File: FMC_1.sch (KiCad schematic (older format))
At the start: 14 parts, among them P1 SAMTEC_ASP-134603-01

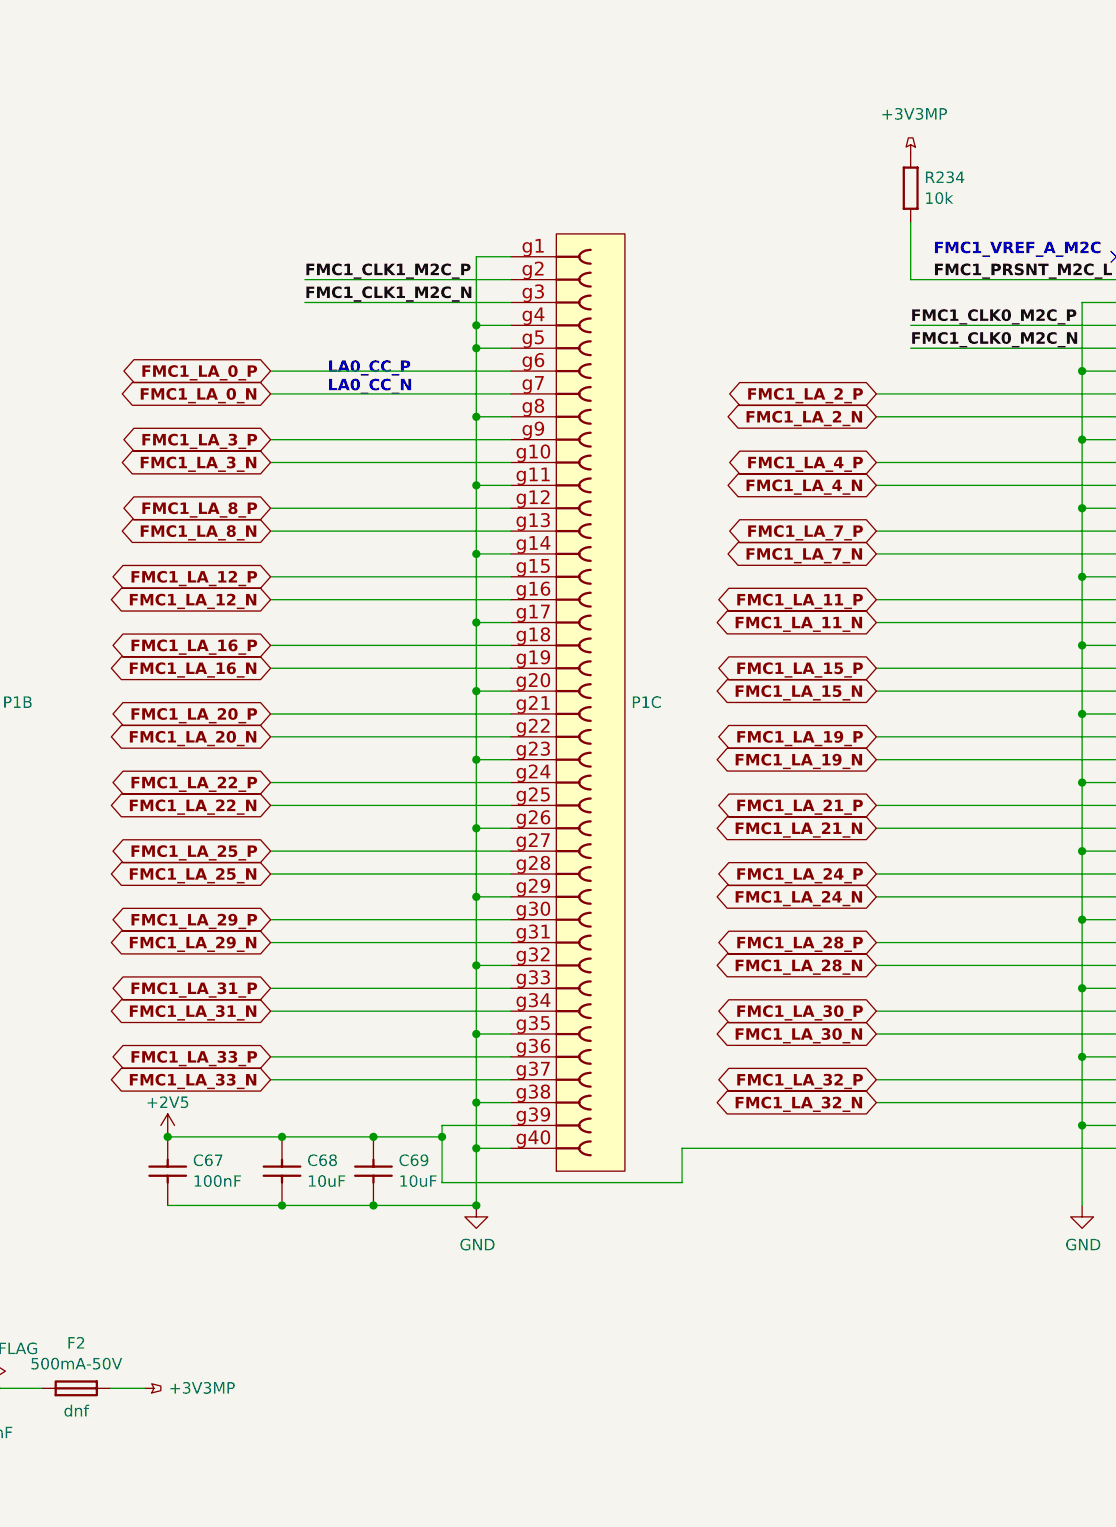
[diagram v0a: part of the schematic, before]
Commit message: SCH: rename +3.3VP, 3V3PM and +3V3MP to +3V3P
  * all of them refer to the same net
  * to make confusion perfect, all 3 power symbols on the schematic
    were an instance of the symbol `+3.3VP` with different
    value attributes
  * renamed the `+3.3VP` symbol to `+3V3P` for naming consistency
  * SCH: replaced all power symbols on the net by the new one
  * PCB: still needs to be synced up, as the net name has changed
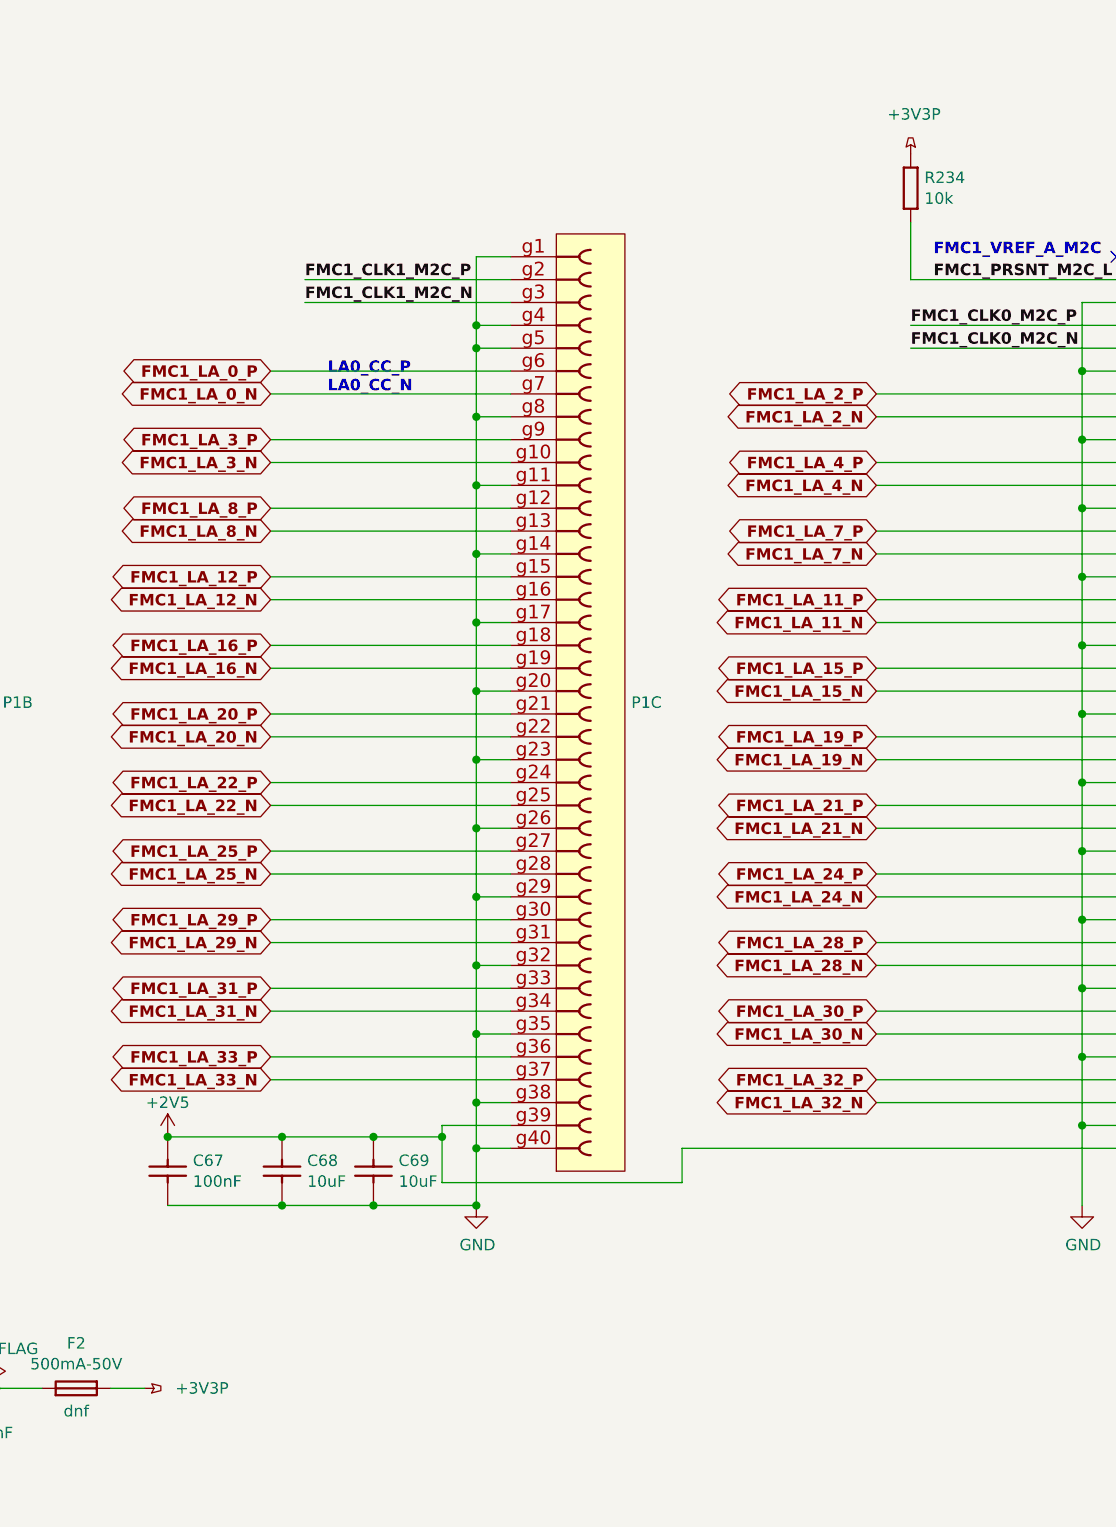
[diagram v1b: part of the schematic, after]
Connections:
- net +3.3VP renamed +3V3P
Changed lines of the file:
@@
 $EndComp
 $Comp
-L power:+3.3VP #PWR?
+L power:+3V3P #PWR?
 U 1 1 5DD348B7
 P 7000 6600
@@
 AR Path="/5DD348B7" Ref="#PWR0550"  Part="1"
 F 0 "#PWR0550" H 7000 6450 50  0001 C CNN
-F 1 "+3V3MP" V 7000 6850 50  0000 C CNN
+F 1 "+3V3P" V 7000 6850 50  0000 C CNN
 F 2 "" H 7000 6600 50  0001 C CNN
 F 3 "" H 7000 6600 50  0001 C CNN
@@
 	10350 1750 11250 1750
 $Comp
-L power:+3.3VP #PWR?
+L power:+3V3P #PWR?
 U 1 1 5E9F763B
 P 10350 1200
@@
 AR Path="/5E9F763B" Ref="#PWR0503"  Part="1"
 F 0 "#PWR0503" H 10350 1050 50  0001 C CNN
-F 1 "+3V3MP" H 10365 1373 50  0000 C CNN
+F 1 "+3V3P" H 10365 1373 50  0000 C CNN
 F 2 "" H 10350 1200 50  0001 C CNN
 F 3 "" H 10350 1200 50  0001 C CNN

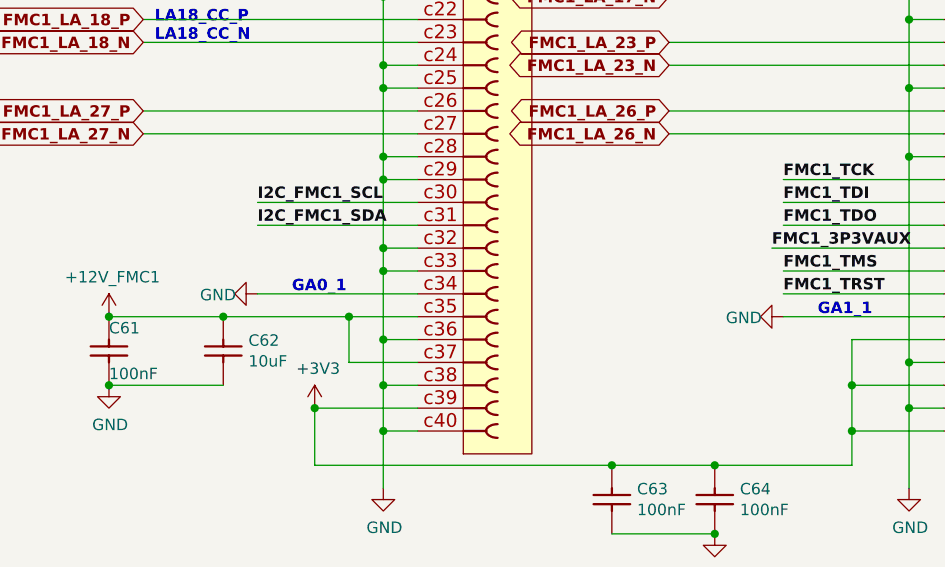
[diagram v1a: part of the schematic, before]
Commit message: Add 300 Ohm series resistors to GA pins
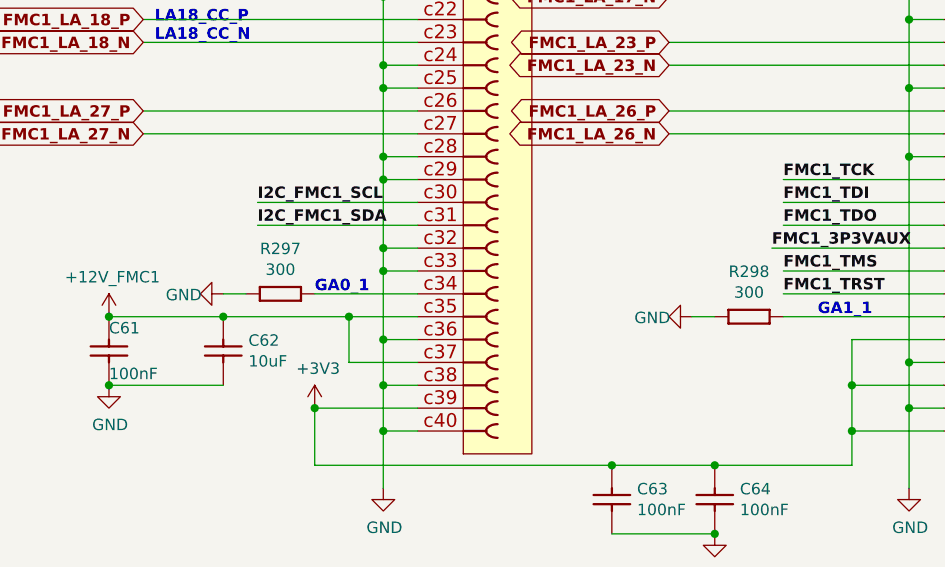
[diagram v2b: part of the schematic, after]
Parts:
- added R297, R298: R0402_300R_1%_0.0625W_100PPM, Resistors SMD:RESC1005X40N, symbol Resistors_SMD:R0402_300R_1%_0.0625W_100PPM
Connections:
- net GND: now also R297.1, R298.1; no longer P1.c34, P1.d35
- new net: P1.c34, R297.2
- new net: P1.d35, R298.2
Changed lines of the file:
@@
 Connection ~ 5450 5550
-Wire Wire Line
-	2850 4950 3550 4950
 Wire Wire Line
 	2850 4550 3550 4550
@@
 Wire Wire Line
 	5150 4850 5850 4850
-Wire Wire Line
-	5150 5050 5850 5050
 Text Notes 4650 3650 0    50   ~ 10
 LA17_CC_P\nLA17_CC_N
@@
 L power:GND #PWR?
 U 1 1 5D17E89A
-P 2850 4950
+P 2700 4950
 AR Path="/5BD32060/5D17E89A" Ref="#PWR?"  Part="1"
 AR Path="/5BD31F9A/5D17E89A" Ref="#PWR0125"  Part="1"
 AR Path="/5BD31F9F/5D17E89A" Ref="#PWR?"  Part="1"
 AR Path="/5D17E89A" Ref="#PWR?"  Part="1"
-F 0 "#PWR0125" H 2850 4700 50  0001 C CNN
-F 1 "GND" V 2855 4777 50  0000 C CNN
-F 2 "" H 2850 4950 50  0001 C CNN
-F 3 "" H 2850 4950 50  0001 C CNN
-	1    2850 4950
+F 0 "#PWR0125" H 2700 4700 50  0001 C CNN
+F 1 "GND" V 2705 4777 50  0000 C CNN
+F 2 "" H 2700 4950 50  0001 C CNN
+F 3 "" H 2700 4950 50  0001 C CNN
+	1    2700 4950
 	0    1    1    0
 $EndComp
@@
 L power:GND #PWR?
 U 1 1 5D19449D
-P 5150 5050
+P 4750 5050
 AR Path="/5BD32060/5D19449D" Ref="#PWR?"  Part="1"
 AR Path="/5BD31F9A/5D19449D" Ref="#PWR0215"  Part="1"
 AR Path="/5BD31F9F/5D19449D" Ref="#PWR?"  Part="1"
 AR Path="/5D19449D" Ref="#PWR?"  Part="1"
-F 0 "#PWR0215" H 5150 4800 50  0001 C CNN
-F 1 "GND" V 5155 4877 50  0000 C CNN
-F 2 "" H 5150 5050 50  0001 C CNN
-F 3 "" H 5150 5050 50  0001 C CNN
-	1    5150 5050
+F 0 "#PWR0215" H 4750 4800 50  0001 C CNN
+F 1 "GND" V 4755 4877 50  0000 C CNN
+F 2 "" H 4750 5050 50  0001 C CNN
+F 3 "" H 4750 5050 50  0001 C CNN
+	1    4750 5050
 	0    1    1    0
 $EndComp
-Text Notes 3000 4950 0    50   ~ 10
+Text Notes 3100 4950 0    50   ~ 10
 GA0_1
 Text Notes 5300 5050 0    50   ~ 10
@@
 Wire Wire Line
 	6350 6600 6550 6600
+$Comp
+L Resistors_SMD:R0402_300R_1%_0.0625W_100PPM R297
+U 1 1 5EBC4ACC
+P 2800 4950
+F 0 "R297" H 2950 5147 50  0000 C CNN
+F 1 "R0402_300R_1%_0.0625W_100PPM" H 2800 4755 50  0001 L CNN
+F 2 "Resistors SMD:RESC1005X40N" H 2800 4680 50  0001 L CNN
+F 3 " " H 2800 4605 50  0001 L CNN
+F 4 "300" H 2950 5056 50  0000 C CNN "Val"
+F 5 "R0402_300R_1%_0.0625W_100PPM" H 2800 4530 50  0001 L CNN "Part Number"
+F 6 "Resistor - 1%" H 2800 4455 50  0001 L CNN "Library Ref"
+F 7 "SchLib\\Resistors.SchLib" H 2800 4380 50  0001 L CNN "Library Path"
+F 8 "300" H 2800 4305 50  0001 L CNN "Comment"
+F 9 "Standard" H 2800 4230 50  0001 L CNN "Component Kind"
+F 10 "Standard" H 2800 4155 50  0001 L CNN "Component Type"
+F 11 " " H 2800 4080 50  0001 L CNN "PackageDescription"
+F 12 "2" H 2800 4005 50  0001 L CNN "Pin Count"
+F 13 "PcbLib\\Resistors SMD.PcbLib" H 2800 3930 50  0001 L CNN "Footprint Path"
+F 14 "RESC1005X40N" H 2800 3855 50  0001 L CNN "Footprint Ref"
+F 15 "Not Recommended" H 2800 3780 50  0001 L CNN "Status"
+F 16 "0.0625W" H 2800 3705 50  0001 L CNN "Power"
+F 17 "±100ppm/°C" H 2800 3630 50  0001 L CNN "TC"
+F 18 " " H 2800 3555 50  0001 L CNN "Voltage"
+F 19 "±1%" H 2800 3480 50  0001 L CNN "Tolerance"
+F 20 "General Purpose Thick Film Chip Resistor" H 2800 3405 50  0001 L CNN "Part Description"
+F 21 "GENERIC" H 2800 3330 50  0001 L CNN "Manufacturer"
+F 22 "R0402_300R_1%_0.0625W_100PPM" H 2800 3255 50  0001 L CNN "Manufacturer Part Number"
+F 23 "0402" H 2800 3180 50  0001 L CNN "Case"
+F 24 "No" H 2800 3105 50  0001 L CNN "PressFit"
+F 25 "Yes" H 2800 3030 50  0001 L CNN "Mounted"
+F 26 " " H 2800 2955 50  0001 L CNN "Sense Comment"
+F 27 "No" H 2800 2880 50  0001 L CNN "Sense"
+F 28 " " H 2800 2805 50  0001 L CNN "Status Comment"
+F 29 "No" H 2800 2730 50  0001 L CNN "Socket"
+F 30 "Yes" H 2800 2655 50  0001 L CNN "SMD"
+F 31 " " H 2800 2580 50  0001 L CNN "ComponentHeight"
+F 32 "YAGEO PHYCOMP" H 2800 2505 50  0001 L CNN "Manufacturer1 Example"
+F 33 "232270673001L" H 2800 2430 50  0001 L CNN "Manufacturer1 Part Number"
+F 34 "0.4mm" H 2800 2355 50  0001 L CNN "Manufacturer1 ComponentHeight"
+F 35 "CERN DEM JLC" H 2800 2280 50  0001 L CNN "Author"
+F 36 "12/03/07 00:00:00" H 2800 2205 50  0001 L CNN "CreateDate"
+F 37 "10/17/12 00:00:00" H 2800 2130 50  0001 L CNN "LatestRevisionDate"
+F 38 "Resistors SMD" H 2800 2055 50  0001 L CNN "Database Table Name"
+F 39 "Resistors.DbLib" H 2800 1980 50  0001 L CNN "Library Name"
+F 40 "Resistors SMD" H 2800 1905 50  0001 L CNN "Footprint Library"
+F 41 "This work is licensed under the Creative Commons CC-BY-SA 4.0 License. To the extent that circuit schematics that use Licensed Material can be considered to be ‘Adapted Material’, then the copyright holder waives article 3.b of the license with respect to these schematics." H 2800 1830 50  0001 L CNN "License"
+	1    2800 4950
+	1    0    0    -1
+$EndComp
+Wire Wire Line
+	2700 4950 2800 4950
+Wire Wire Line
+	3100 4950 3550 4950
+$Comp
+L Resistors_SMD:R0402_300R_1%_0.0625W_100PPM R298
+U 1 1 5ECB9FE8
+P 4850 5050
+F 0 "R298" H 5000 5247 50  0000 C CNN
+F 1 "R0402_300R_1%_0.0625W_100PPM" H 4850 4855 50  0001 L CNN
+F 2 "Resistors SMD:RESC1005X40N" H 4850 4780 50  0001 L CNN
+F 3 " " H 4850 4705 50  0001 L CNN
+F 4 "300" H 5000 5156 50  0000 C CNN "Val"
+F 5 "R0402_300R_1%_0.0625W_100PPM" H 4850 4630 50  0001 L CNN "Part Number"
+F 6 "Resistor - 1%" H 4850 4555 50  0001 L CNN "Library Ref"
+F 7 "SchLib\\Resistors.SchLib" H 4850 4480 50  0001 L CNN "Library Path"
+F 8 "300" H 4850 4405 50  0001 L CNN "Comment"
+F 9 "Standard" H 4850 4330 50  0001 L CNN "Component Kind"
+F 10 "Standard" H 4850 4255 50  0001 L CNN "Component Type"
+F 11 " " H 4850 4180 50  0001 L CNN "PackageDescription"
+F 12 "2" H 4850 4105 50  0001 L CNN "Pin Count"
+F 13 "PcbLib\\Resistors SMD.PcbLib" H 4850 4030 50  0001 L CNN "Footprint Path"
+F 14 "RESC1005X40N" H 4850 3955 50  0001 L CNN "Footprint Ref"
+F 15 "Not Recommended" H 4850 3880 50  0001 L CNN "Status"
+F 16 "0.0625W" H 4850 3805 50  0001 L CNN "Power"
+F 17 "±100ppm/°C" H 4850 3730 50  0001 L CNN "TC"
+F 18 " " H 4850 3655 50  0001 L CNN "Voltage"
+F 19 "±1%" H 4850 3580 50  0001 L CNN "Tolerance"
+F 20 "General Purpose Thick Film Chip Resistor" H 4850 3505 50  0001 L CNN "Part Description"
+F 21 "GENERIC" H 4850 3430 50  0001 L CNN "Manufacturer"
+F 22 "R0402_300R_1%_0.0625W_100PPM" H 4850 3355 50  0001 L CNN "Manufacturer Part Number"
+F 23 "0402" H 4850 3280 50  0001 L CNN "Case"
+F 24 "No" H 4850 3205 50  0001 L CNN "PressFit"
+F 25 "Yes" H 4850 3130 50  0001 L CNN "Mounted"
+F 26 " " H 4850 3055 50  0001 L CNN "Sense Comment"
+F 27 "No" H 4850 2980 50  0001 L CNN "Sense"
+F 28 " " H 4850 2905 50  0001 L CNN "Status Comment"
+F 29 "No" H 4850 2830 50  0001 L CNN "Socket"
+F 30 "Yes" H 4850 2755 50  0001 L CNN "SMD"
+F 31 " " H 4850 2680 50  0001 L CNN "ComponentHeight"
+F 32 "YAGEO PHYCOMP" H 4850 2605 50  0001 L CNN "Manufacturer1 Example"
+F 33 "232270673001L" H 4850 2530 50  0001 L CNN "Manufacturer1 Part Number"
+F 34 "0.4mm" H 4850 2455 50  0001 L CNN "Manufacturer1 ComponentHeight"
+F 35 "CERN DEM JLC" H 4850 2380 50  0001 L CNN "Author"
+F 36 "12/03/07 00:00:00" H 4850 2305 50  0001 L CNN "CreateDate"
+F 37 "10/17/12 00:00:00" H 4850 2230 50  0001 L CNN "LatestRevisionDate"
+F 38 "Resistors SMD" H 4850 2155 50  0001 L CNN "Database Table Name"
+F 39 "Resistors.DbLib" H 4850 2080 50  0001 L CNN "Library Name"
+F 40 "Resistors SMD" H 4850 2005 50  0001 L CNN "Footprint Library"
+F 41 "This work is licensed under the Creative Commons CC-BY-SA 4.0 License. To the extent that circuit schematics that use Licensed Material can be considered to be ‘Adapted Material’, then the copyright holder waives article 3.b of the license with respect to these schematics." H 4850 1930 50  0001 L CNN "License"
+	1    4850 5050
+	1    0    0    -1
+$EndComp
+Wire Wire Line
+	4750 5050 4850 5050
+Wire Wire Line
+	5150 5050 5850 5050
 $EndSCHEMATC

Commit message: change R297 - R300 to 240 Ohm
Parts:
- R297, R298: value R0402_300R_1%_0.0625W_100PPM -> R0402_240R_1%_0.0625W_100PPM; footprint Resistors SMD:RESC1005X40N -> Marble:RESC1005X40N; symbol Resistors_SMD:R0402_300R_1%_0.0625W_100PPM -> Resistors_SMD:R0402_240R_1%_0.0625W_100PPM; Comment 300 -> 240; Manufacturer Part Number R0402_300R_1%_0.0625W_100PPM -> R0402_240R_1%_0.0625W_100PPM; Manufacturer1 Part Number 232270673001L -> 232270672401L; Part Number R0402_300R_1%_0.0625W_100PPM -> R0402_240R_1%_0.0625W_100PPM; Val 300 -> 240
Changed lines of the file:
@@
 	6350 6600 6550 6600
 $Comp
-L Resistors_SMD:R0402_300R_1%_0.0625W_100PPM R297
+L Resistors_SMD:R0402_240R_1%_0.0625W_100PPM R297
 U 1 1 5EBC4ACC
 P 2800 4950
 F 0 "R297" H 2950 5147 50  0000 C CNN
-F 1 "R0402_300R_1%_0.0625W_100PPM" H 2800 4755 50  0001 L CNN
-F 2 "Resistors SMD:RESC1005X40N" H 2800 4680 50  0001 L CNN
+F 1 "R0402_240R_1%_0.0625W_100PPM" H 2800 4755 50  0001 L CNN
+F 2 "Marble:RESC1005X40N" H 2800 4680 50  0001 L CNN
 F 3 " " H 2800 4605 50  0001 L CNN
-F 4 "300" H 2950 5056 50  0000 C CNN "Val"
-F 5 "R0402_300R_1%_0.0625W_100PPM" H 2800 4530 50  0001 L CNN "Part Number"
+F 4 "240" H 2950 5056 50  0000 C CNN "Val"
+F 5 "R0402_240R_1%_0.0625W_100PPM" H 2800 4530 50  0001 L CNN "Part Number"
 F 6 "Resistor - 1%" H 2800 4455 50  0001 L CNN "Library Ref"
 F 7 "SchLib\\Resistors.SchLib" H 2800 4380 50  0001 L CNN "Library Path"
-F 8 "300" H 2800 4305 50  0001 L CNN "Comment"
+F 8 "240" H 2800 4305 50  0001 L CNN "Comment"
 F 9 "Standard" H 2800 4230 50  0001 L CNN "Component Kind"
 F 10 "Standard" H 2800 4155 50  0001 L CNN "Component Type"
@@
 F 20 "General Purpose Thick Film Chip Resistor" H 2800 3405 50  0001 L CNN "Part Description"
 F 21 "GENERIC" H 2800 3330 50  0001 L CNN "Manufacturer"
-F 22 "R0402_300R_1%_0.0625W_100PPM" H 2800 3255 50  0001 L CNN "Manufacturer Part Number"
+F 22 "R0402_240R_1%_0.0625W_100PPM" H 2800 3255 50  0001 L CNN "Manufacturer Part Number"
 F 23 "0402" H 2800 3180 50  0001 L CNN "Case"
 F 24 "No" H 2800 3105 50  0001 L CNN "PressFit"
@@
 F 31 " " H 2800 2580 50  0001 L CNN "ComponentHeight"
 F 32 "YAGEO PHYCOMP" H 2800 2505 50  0001 L CNN "Manufacturer1 Example"
-F 33 "232270673001L" H 2800 2430 50  0001 L CNN "Manufacturer1 Part Number"
+F 33 "232270672401L" H 2800 2430 50  0001 L CNN "Manufacturer1 Part Number"
 F 34 "0.4mm" H 2800 2355 50  0001 L CNN "Manufacturer1 ComponentHeight"
 F 35 "CERN DEM JLC" H 2800 2280 50  0001 L CNN "Author"
@@
 	3100 4950 3550 4950
 $Comp
-L Resistors_SMD:R0402_300R_1%_0.0625W_100PPM R298
+L Resistors_SMD:R0402_240R_1%_0.0625W_100PPM R298
 U 1 1 5ECB9FE8
 P 4850 5050
 F 0 "R298" H 5000 5247 50  0000 C CNN
-F 1 "R0402_300R_1%_0.0625W_100PPM" H 4850 4855 50  0001 L CNN
-F 2 "Resistors SMD:RESC1005X40N" H 4850 4780 50  0001 L CNN
+F 1 "R0402_240R_1%_0.0625W_100PPM" H 4850 4855 50  0001 L CNN
+F 2 "Marble:RESC1005X40N" H 4850 4780 50  0001 L CNN
 F 3 " " H 4850 4705 50  0001 L CNN
-F 4 "300" H 5000 5156 50  0000 C CNN "Val"
-F 5 "R0402_300R_1%_0.0625W_100PPM" H 4850 4630 50  0001 L CNN "Part Number"
+F 4 "240" H 5000 5156 50  0000 C CNN "Val"
+F 5 "R0402_240R_1%_0.0625W_100PPM" H 4850 4630 50  0001 L CNN "Part Number"
 F 6 "Resistor - 1%" H 4850 4555 50  0001 L CNN "Library Ref"
 F 7 "SchLib\\Resistors.SchLib" H 4850 4480 50  0001 L CNN "Library Path"
-F 8 "300" H 4850 4405 50  0001 L CNN "Comment"
+F 8 "240" H 4850 4405 50  0001 L CNN "Comment"
 F 9 "Standard" H 4850 4330 50  0001 L CNN "Component Kind"
 F 10 "Standard" H 4850 4255 50  0001 L CNN "Component Type"
@@
 F 20 "General Purpose Thick Film Chip Resistor" H 4850 3505 50  0001 L CNN "Part Description"
 F 21 "GENERIC" H 4850 3430 50  0001 L CNN "Manufacturer"
-F 22 "R0402_300R_1%_0.0625W_100PPM" H 4850 3355 50  0001 L CNN "Manufacturer Part Number"
+F 22 "R0402_240R_1%_0.0625W_100PPM" H 4850 3355 50  0001 L CNN "Manufacturer Part Number"
 F 23 "0402" H 4850 3280 50  0001 L CNN "Case"
 F 24 "No" H 4850 3205 50  0001 L CNN "PressFit"
@@
 F 31 " " H 4850 2680 50  0001 L CNN "ComponentHeight"
 F 32 "YAGEO PHYCOMP" H 4850 2605 50  0001 L CNN "Manufacturer1 Example"
-F 33 "232270673001L" H 4850 2530 50  0001 L CNN "Manufacturer1 Part Number"
+F 33 "232270672401L" H 4850 2530 50  0001 L CNN "Manufacturer1 Part Number"
 F 34 "0.4mm" H 4850 2455 50  0001 L CNN "Manufacturer1 ComponentHeight"
 F 35 "CERN DEM JLC" H 4850 2380 50  0001 L CNN "Author"
